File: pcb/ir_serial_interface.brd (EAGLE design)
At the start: 41.9 x 25.4 mm, 34 parts, among them IC1 PIC18LF2550, IC2 LP2992, T1 PS401

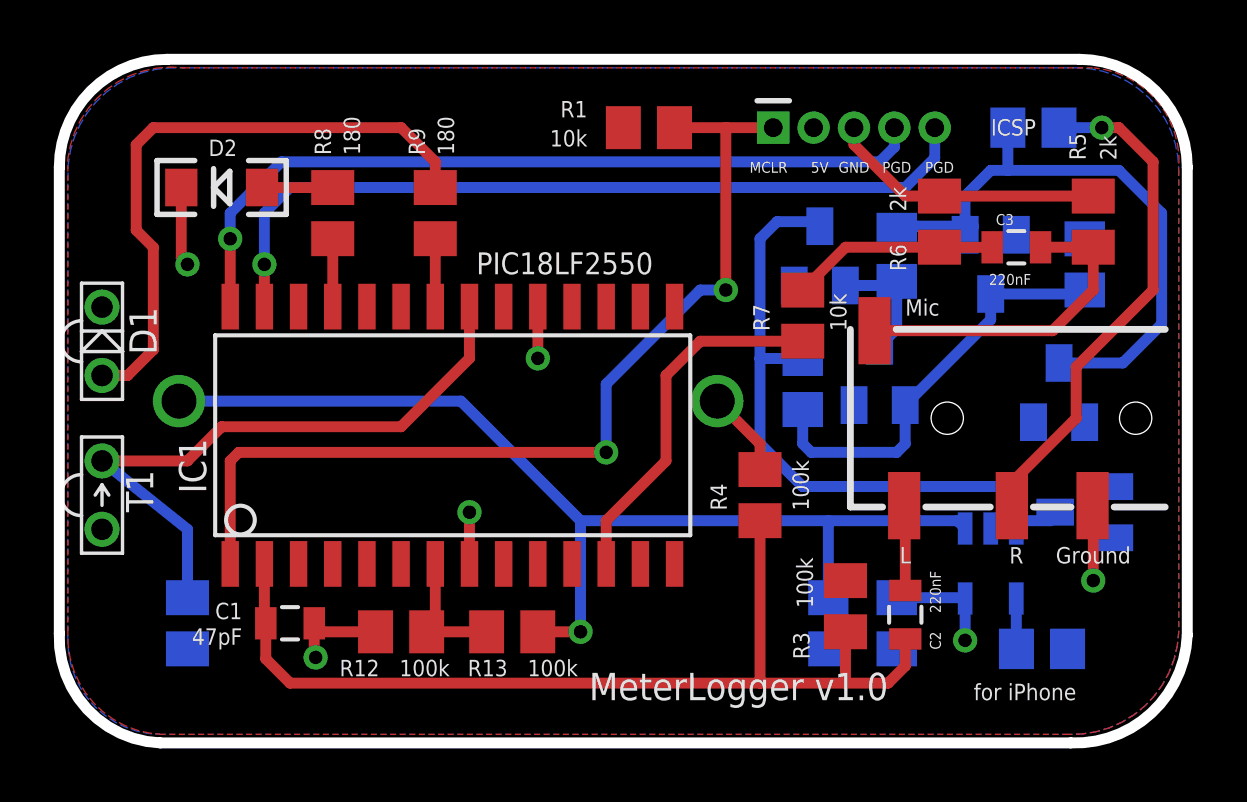
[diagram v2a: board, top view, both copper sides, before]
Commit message: PCB: fix
comparator was connected to battery/2 instead ov 5V/2
version 1.0.1
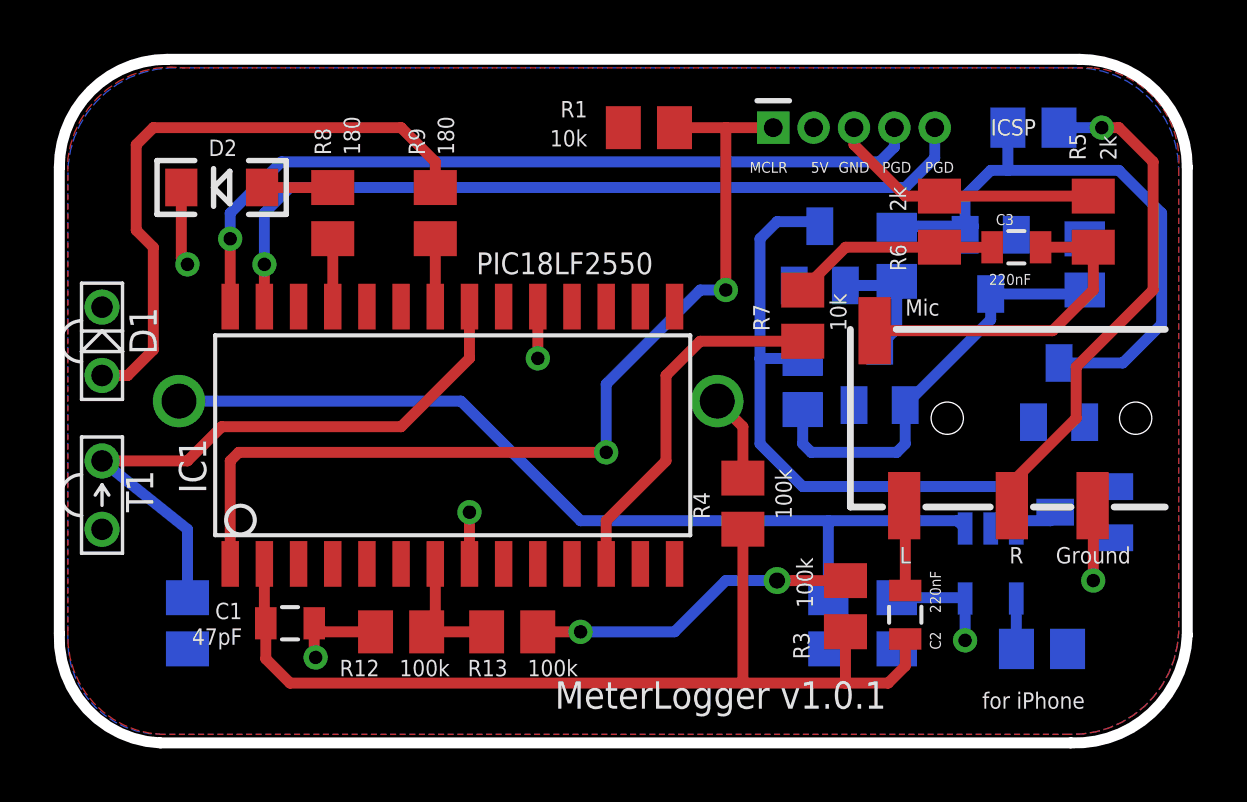
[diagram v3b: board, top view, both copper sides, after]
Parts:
- moved R4 0.71 mm to (47.3, 34.3)
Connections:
- net +5V: now also R13.2
- net V+: no longer R13.2
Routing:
- net +5V: track 4.11 -> 16.3 mm, vias 1 -> 3
- net V+: track 39.7 -> 34.0 mm, vias 1 -> 0
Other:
- board text added: "MeterLogger v1.0.1"
- board text removed: "MeterLogger v1.0"
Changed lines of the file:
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@@
 <layers>
 <layer number="1" name="Top" color="4" fill="1" visible="yes" active="yes"/>
-<layer number="16" name="Bottom" color="1" fill="1" visible="yes" active="yes"/>
+<layer number="16" name="Bottom" color="1" fill="1" visible="no" active="yes"/>
 <layer number="17" name="Pads" color="2" fill="1" visible="yes" active="yes"/>
 <layer number="18" name="Vias" color="2" fill="1" visible="yes" active="yes"/>
@@
 <plain>
 <text x="35.56" y="38.1" size="1.016" layer="122" ratio="10" rot="MR270" align="bottom-center">2 x CR2032</text>
-<text x="41.5925" y="26.9875" size="1.016" layer="121" ratio="10">MeterLogger v1.0</text>
+<text x="40.3225" y="26.67" size="1.016" layer="121" ratio="10">MeterLogger v1.0.1</text>
 <text x="60.0075" y="27.305" size="0.4064" layer="122" rot="MR0">(C) 2014, Kristoffer Ek + Johannes Gaardsted Jørgensen</text>
 <text x="56.515" y="48.5775" size="0.6096" layer="121" ratio="10" rot="R180" align="bottom-right">ICSP</text>
@@
 <wire x1="21.9075" y1="29.4692875" x2="21.9075" y2="46.78993125" width="0.4064" layer="20"/>
 <wire x1="21.9075" y1="46.78993125" x2="25.91756875" y2="50.8" width="0.4064" layer="20" curve="-90"/>
-<text x="55.88" y="26.9875" size="0.6096" layer="121" ratio="10">for iPhone</text>
+<text x="56.1975" y="26.67" size="0.6096" layer="121" ratio="10">for iPhone</text>
 <text x="53.34" y="32.0675" size="0.6096" layer="121" ratio="10" align="bottom-center">L</text>
 <text x="53.34" y="41.275" size="0.6096" layer="121" ratio="10">Mic</text>
@@
 <attribute name="VALUE" x="61.9125" y="45.72" size="0.6096" layer="26" rot="MR270"/>
 </element>
-<element name="R4" library="resistor" package="M0805" value="100k" x="47.9425" y="34.6075" smashed="yes" rot="R270">
-<attribute name="NAME" x="46.101" y="34.036" size="0.6096" layer="25" rot="R270" align="bottom-right"/>
-<attribute name="VALUE" x="49.149" y="34.036" size="0.6096" layer="25" rot="R270" align="bottom-right"/>
+<element name="R4" library="resistor" package="M0805" value="100k" x="47.3075" y="34.29" smashed="yes" rot="R270">
+<attribute name="NAME" x="45.466" y="33.7185" size="0.6096" layer="25" rot="R270" align="bottom-right"/>
+<attribute name="VALUE" x="48.514" y="33.7185" size="0.6096" layer="25" rot="R270" align="bottom-right"/>
 </element>
 <element name="U$2" library="SparkFun-Connectors" package="AUDIO-JACK-TRRS-SMD" value="AUDIO-JACK3" x="63.5" y="37.465" rot="R180"/>
@@
 <wire x1="53.0225" y1="30.795" x2="55.5375" y2="30.795" width="0.4064" layer="16"/>
 <wire x1="55.5375" y1="30.795" x2="55.565" y2="30.7675" width="0.4064" layer="16"/>
+<contactref element="R13" pad="2"/>
+<wire x1="39.685" y1="29.5275" x2="41.275" y2="29.5275" width="0.4064" layer="1"/>
+<via x="41.275" y="29.5275" extent="1-16" drill="0.5"/>
+<wire x1="51.1175" y1="31.43" x2="49.215" y2="31.43" width="0.4064" layer="1"/>
+<wire x1="49.215" y1="31.43" x2="48.5775" y2="31.4325" width="0.4064" layer="1"/>
+<via x="48.5775" y="31.4325" extent="1-16" drill="0.6"/>
+<wire x1="48.5775" y1="31.4325" x2="46.6725" y2="31.4325" width="0.4064" layer="16"/>
+<wire x1="46.6725" y1="31.4325" x2="44.7675" y2="29.5275" width="0.4064" layer="16"/>
+<wire x1="44.7675" y1="29.5275" x2="41.275" y2="29.5275" width="0.4064" layer="16"/>
 </signal>
 <signal name="GND">
@@
 <wire x1="31.38" y1="28.6275" x2="31.4325" y2="28.575" width="0.4064" layer="1"/>
 <via x="31.4325" y="28.575" extent="1-16" drill="0.5"/>
-<wire x1="46.355" y1="38.1" x2="47.9425" y2="36.5125" width="0.4064" layer="1"/>
-<wire x1="47.9425" y1="36.5125" x2="47.9425" y2="35.5575" width="0.4064" layer="1"/>
+<wire x1="46.355" y1="38.1" x2="47.3075" y2="37.1475" width="0.4064" layer="1"/>
+<wire x1="47.3075" y1="37.1475" x2="47.3075" y2="35.24" width="0.4064" layer="1"/>
 <wire x1="60.3" y1="34.215" x2="60.325" y2="34.215" width="0.4064" layer="1"/>
 <wire x1="60.325" y1="34.215" x2="60.325" y2="31.4325" width="0.4064" layer="1"/>
@@
 <wire x1="29.58" y1="29.845" x2="29.58" y2="28.5225" width="0.4064" layer="1"/>
 <wire x1="29.58" y1="28.5225" x2="30.48" y2="27.6225" width="0.4064" layer="1"/>
-<wire x1="30.48" y1="27.6225" x2="47.9425" y2="27.6225" width="0.4064" layer="1"/>
-<wire x1="47.9425" y1="27.6225" x2="51.1175" y2="27.6225" width="0.4064" layer="1"/>
+<wire x1="30.48" y1="27.6225" x2="47.3075" y2="27.6225" width="0.4064" layer="1"/>
+<wire x1="47.3075" y1="27.6225" x2="51.1175" y2="27.6225" width="0.4064" layer="1"/>
 <wire x1="51.1175" y1="27.6225" x2="52.705" y2="27.6225" width="0.4064" layer="1"/>
 <wire x1="52.705" y1="27.6225" x2="53.34" y2="28.2575" width="0.4064" layer="1"/>
 <wire x1="53.34" y1="28.2575" x2="53.34" y2="29.2625" width="0.4064" layer="1"/>
 <wire x1="51.1175" y1="29.53" x2="51.1175" y2="27.6225" width="0.4064" layer="1"/>
-<wire x1="47.9425" y1="33.6575" x2="47.9425" y2="27.6225" width="0.4064" layer="1"/>
+<wire x1="47.3075" y1="33.34" x2="47.3075" y2="27.6225" width="0.4064" layer="1"/>
 </signal>
 <signal name="N$7">
@@
 <contactref element="BAT1" pad="1"/>
 <contactref element="IC2" pad="1"/>
-<contactref element="R13" pad="2"/>
 <wire x1="26.355" y1="38.1" x2="36.83" y2="38.1" width="0.4064" layer="16"/>
 <wire x1="36.83" y1="38.1" x2="41.275" y2="33.655" width="0.4064" layer="16"/>
-<wire x1="39.685" y1="29.5275" x2="41.275" y2="29.5275" width="0.4064" layer="1"/>
-<via x="41.275" y="29.5275" extent="1-16" drill="0.5"/>
-<wire x1="41.275" y1="29.5275" x2="41.275" y2="33.655" width="0.4064" layer="16"/>
 <contactref element="C6" pad="1"/>
 <wire x1="41.275" y1="33.655" x2="50.4825" y2="33.655" width="0.4064" layer="16"/>

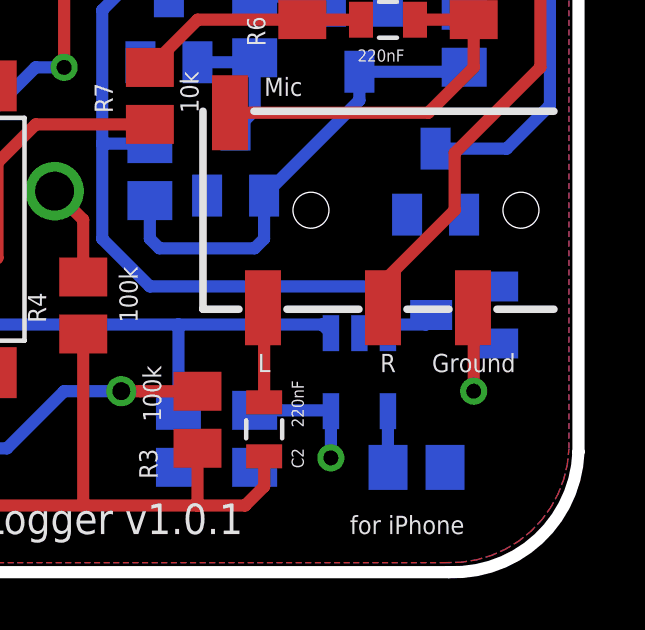
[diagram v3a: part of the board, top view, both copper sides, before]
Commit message: PCB: no zener
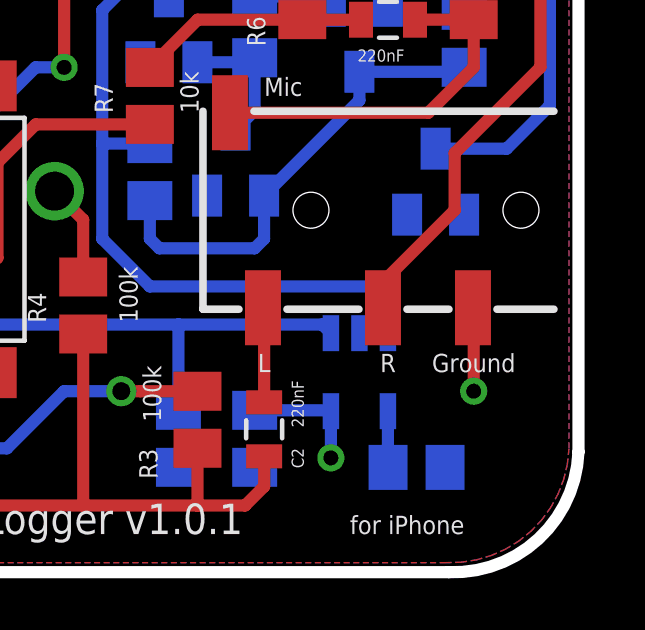
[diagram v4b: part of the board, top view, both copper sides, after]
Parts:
- removed D7: MMBZ5231BLT1G, diode:SOT23
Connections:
- net GND: no longer D7.1
- net N$21: no longer D7.3
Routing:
- net N$21: track 25.3 -> 23.3 mm
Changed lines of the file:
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@@
 <layers>
 <layer number="1" name="Top" color="4" fill="1" visible="yes" active="yes"/>
-<layer number="16" name="Bottom" color="1" fill="1" visible="no" active="yes"/>
+<layer number="16" name="Bottom" color="1" fill="1" visible="yes" active="yes"/>
 <layer number="17" name="Pads" color="2" fill="1" visible="yes" active="yes"/>
 <layer number="18" name="Vias" color="2" fill="1" visible="yes" active="yes"/>
@@
 <layer number="20" name="Dimension" color="15" fill="1" visible="yes" active="yes"/>
 <layer number="21" name="tPlace" color="7" fill="1" visible="yes" active="yes"/>
-<layer number="22" name="bPlace" color="7" fill="1" visible="no" active="yes"/>
+<layer number="22" name="bPlace" color="7" fill="1" visible="yes" active="yes"/>
 <layer number="23" name="tOrigins" color="15" fill="1" visible="yes" active="yes"/>
-<layer number="24" name="bOrigins" color="15" fill="1" visible="no" active="yes"/>
+<layer number="24" name="bOrigins" color="15" fill="1" visible="yes" active="yes"/>
 <layer number="25" name="tNames" color="7" fill="1" visible="yes" active="yes"/>
-<layer number="26" name="bNames" color="7" fill="1" visible="no" active="yes"/>
+<layer number="26" name="bNames" color="7" fill="1" visible="yes" active="yes"/>
 <layer number="27" name="tValues" color="7" fill="1" visible="yes" active="yes"/>
-<layer number="28" name="bValues" color="7" fill="1" visible="no" active="yes"/>
+<layer number="28" name="bValues" color="7" fill="1" visible="yes" active="yes"/>
 <layer number="29" name="tStop" color="7" fill="3" visible="yes" active="yes"/>
-<layer number="30" name="bStop" color="7" fill="6" visible="no" active="yes"/>
+<layer number="30" name="bStop" color="7" fill="6" visible="yes" active="yes"/>
 <layer number="31" name="tCream" color="7" fill="4" visible="yes" active="yes"/>
-<layer number="32" name="bCream" color="7" fill="5" visible="no" active="yes"/>
+<layer number="32" name="bCream" color="7" fill="5" visible="yes" active="yes"/>
 <layer number="33" name="tFinish" color="6" fill="3" visible="yes" active="yes"/>
-<layer number="34" name="bFinish" color="6" fill="6" visible="no" active="yes"/>
+<layer number="34" name="bFinish" color="6" fill="6" visible="yes" active="yes"/>
 <layer number="35" name="tGlue" color="7" fill="4" visible="yes" active="yes"/>
-<layer number="36" name="bGlue" color="7" fill="5" visible="no" active="yes"/>
+<layer number="36" name="bGlue" color="7" fill="5" visible="yes" active="yes"/>
 <layer number="37" name="tTest" color="7" fill="1" visible="yes" active="yes"/>
-<layer number="38" name="bTest" color="7" fill="1" visible="no" active="yes"/>
+<layer number="38" name="bTest" color="7" fill="1" visible="yes" active="yes"/>
 <layer number="39" name="tKeepout" color="4" fill="11" visible="yes" active="yes"/>
-<layer number="40" name="bKeepout" color="1" fill="11" visible="no" active="yes"/>
+<layer number="40" name="bKeepout" color="1" fill="11" visible="yes" active="yes"/>
 <layer number="41" name="tRestrict" color="4" fill="10" visible="yes" active="yes"/>
-<layer number="42" name="bRestrict" color="1" fill="10" visible="no" active="yes"/>
+<layer number="42" name="bRestrict" color="1" fill="10" visible="yes" active="yes"/>
 <layer number="43" name="vRestrict" color="2" fill="10" visible="yes" active="yes"/>
 <layer number="44" name="Drills" color="7" fill="1" visible="yes" active="yes"/>
@@
 <layer number="50" name="dxf" color="7" fill="1" visible="no" active="no"/>
 <layer number="51" name="tDocu" color="7" fill="1" visible="yes" active="yes"/>
-<layer number="52" name="bDocu" color="7" fill="1" visible="no" active="yes"/>
+<layer number="52" name="bDocu" color="7" fill="1" visible="yes" active="yes"/>
 <layer number="53" name="tGND_GNDA" color="7" fill="9" visible="no" active="no"/>
 <layer number="54" name="bGND_GNDA" color="1" fill="9" visible="no" active="no"/>
@@
 <layer number="104" name="Name" color="16" fill="1" visible="yes" active="yes"/>
 <layer number="105" name="tPlate" color="7" fill="1" visible="yes" active="yes"/>
-<layer number="106" name="bPlate" color="7" fill="1" visible="no" active="yes"/>
+<layer number="106" name="bPlate" color="7" fill="1" visible="yes" active="yes"/>
 <layer number="107" name="Crop" color="7" fill="1" visible="yes" active="yes"/>
 <layer number="108" name="tplace-old" color="10" fill="1" visible="no" active="yes"/>
@@
 <layer number="116" name="Patch_BOT" color="9" fill="4" visible="yes" active="yes"/>
 <layer number="121" name="_tsilk" color="7" fill="1" visible="yes" active="yes"/>
-<layer number="122" name="_bsilk" color="7" fill="1" visible="no" active="yes"/>
+<layer number="122" name="_bsilk" color="7" fill="1" visible="yes" active="yes"/>
 <layer number="123" name="tTestmark" color="7" fill="1" visible="no" active="yes"/>
 <layer number="124" name="bTestmark" color="7" fill="1" visible="no" active="yes"/>
@@
 <attribute name="VALUE" x="48.26" y="36.195" size="0.6096" layer="26" rot="MR0" align="bottom-right"/>
 </element>
-<element name="D7" library="diode" package="SOT23" value="MMBZ5231BLT1G" x="60.0075" y="33.9725" smashed="yes" rot="MR270">
-<attribute name="NAME" x="58.42" y="34.925" size="0.6096" layer="26" rot="MR90"/>
-<attribute name="VALUE" x="62.23" y="35.56" size="0.6096" layer="26" rot="MR270" align="top-left"/>
-</element>
 </elements>
 <signals>
@@
 <contactref element="D3" pad="1"/>
 <contactref element="C8" pad="1"/>
-<contactref element="D7" pad="1"/>
 <wire x1="54.61" y1="45.7175" x2="53.3425" y2="45.7175" width="0.4064" layer="1"/>
 <wire x1="53.3425" y1="45.7175" x2="51.435" y2="47.625" width="0.4064" layer="1"/>
@@
 <contactref element="D6" pad="3"/>
 <contactref element="IC2" pad="3"/>
-<contactref element="D7" pad="3"/>
-<wire x1="58.9075" y1="33.9725" x2="59.055" y2="33.9725" width="0.4064" layer="16"/>
-<wire x1="59.055" y1="33.9725" x2="58.7375" y2="33.655" width="0.4064" layer="16"/>
-<wire x1="58.7375" y1="33.655" x2="57.7525" y2="33.655" width="0.4064" layer="16"/>
-<wire x1="57.7525" y1="33.655" x2="57.465" y2="33.3675" width="0.4064" layer="16"/>
 <wire x1="57.465" y1="33.3675" x2="57.465" y2="34.61" width="0.4064" layer="16"/>
 <wire x1="57.465" y1="34.61" x2="57.15" y2="34.925" width="0.4064" layer="16"/>
